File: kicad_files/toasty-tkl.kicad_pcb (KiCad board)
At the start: 2 copper layers, 345.7 x 134.1 mm, 195 parts, among them CON1 USB-MINI-B, SW0:0 ESC, SW0:10 F9, SW0:11 F10, SW0:12 F11, SW0:13 F12, SW0:14 PRINT, SW0:15 SCROLL LOCK, SW0:2 F1, SW0:3 F2, SW0:4 F3, SW0:5 F4, SW0:6 F5, SW0:7 F6, SW0:8 F7, SW0:9 F8, SW1:0 `, SW1:1 1, SW1:10 0, SW1:11 -, SW1:12 =, SW1:13 BACK SPACE, SW1:14 INSERT, SW1:15 HOME, SW1:2 2, SW1:3 3, SW1:4 4, SW1:5 5, SW1:6 6, SW1:7 7, SW1:8 8, SW1:9 9, SW2:0 TAB, SW2:1 Q, SW2:10 P, SW2:11 [, SW2:12 ], SW2:13 \, SW2:14 DELETE, SW2:15 END, SW2:2 W, SW2:3 E, SW2:4 R, SW2:5 T, SW2:6 Y, SW2:7 U, SW2:8 I, SW2:9 O, SW3:0 CAPS LOCK, SW3:1 A, SW3:10 ;, SW3:11 ', SW3:13 ENTER, SW3:14 PAGE UP, SW3:15 PAUSE, SW3:2 S, SW3:3 D, SW3:4 F, SW3:5 G, SW3:6 H, SW3:7 J, SW3:8 K, SW3:9 L, SW4:0 LEFT SHIFT, SW4:1 Z, SW4:10 /, SW4:13 RIGHT SHIFT, SW4:14 PAGE DOWN, SW4:15 UP, SW4:2 X, SW4:3 C, SW4:4 V, SW4:5 B, SW4:6 N, SW4:7 M, SW4:8 ,, SW4:9 ., SW5:0 LEFT CTRL, SW5:1 LEFT WINDOWS, SW5:10 RIGHT WINDOWS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

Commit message: Added GPL and killed some bogus cache files.
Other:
- board text added: "'"
- board text added: ","
- board text added: "-"
- board text added: "."
- board text added: "/"
- board text added: "0"
- board text added: "1"
- board text added: "2"
- board text added: "3"
- board text added: "4"
- board text added: "5"
- board text added: "6"
- board text added: "7"
- board text added: "8"
- board text added: "9"
- board text added: ";"
- board text added: "="
- board text added: "A"
- board text added: "B"
- board text added: "BACK SPACE"
- board text added: "C"
- board text added: "CAPS LOCK"
- board text added: "D"
- board text added: "DELETE"
- board text added: "DOWN"
- board text added: "E"
- board text added: "END"
- board text added: "ENTER"
- board text added: "ESC"
- board text added: "F"
- board text added: "F1"
- board text added: "F10"
- board text added: "F11"
- board text added: "F12"
- board text added: "F2"
- board text added: "F3"
- board text added: "F4"
- board text added: "F5"
- board text added: "F6"
- board text added: "F7"
- board text added: "F9"
- board text added: "G"
- board text added: "H"
- board text added: "HOME"
- board text added: "I"
- board text added: "INSERT"
- board text added: "J"
- board text added: "K"
- board text added: "L"
- board text added: "L ALT"
- board text added: "L CTRL"
- board text added: "L SHIFT"
- board text added: "L WIN"
- board text added: "LEFT"
- board text added: "M"
- board text added: "MENU"
- board text added: "N"
- board text added: "O"
- board text added: "P"
- board text added: "PAUSE"
- board text added: "PG DN"
- board text added: "PG UP"
- board text added: "PRT SC"
- board text added: "Q"
- board text added: "R"
- board text added: "R ALT"
- board text added: "R CTRL"
- board text added: "R SHIFT"
- board text added: "R WIN"
- board text added: "RIGHT"
- board text added: "S"
- board text added: "SCROLL LOCK"
- board text added: "SPACE"
- board text added: "T"
- board text added: "TAB"
- board text added: "ToastyTKL"
- board text added: "U"
- board text added: "UP"
- board text added: "V"
- board text added: "W"
- board text added: "X"
- board text added: "Y"
- board text added: "Z"
- board text added: "["
- board text added: "\"
- board text added: "]"
- board text added: "`"
- board text added: "rev 1"

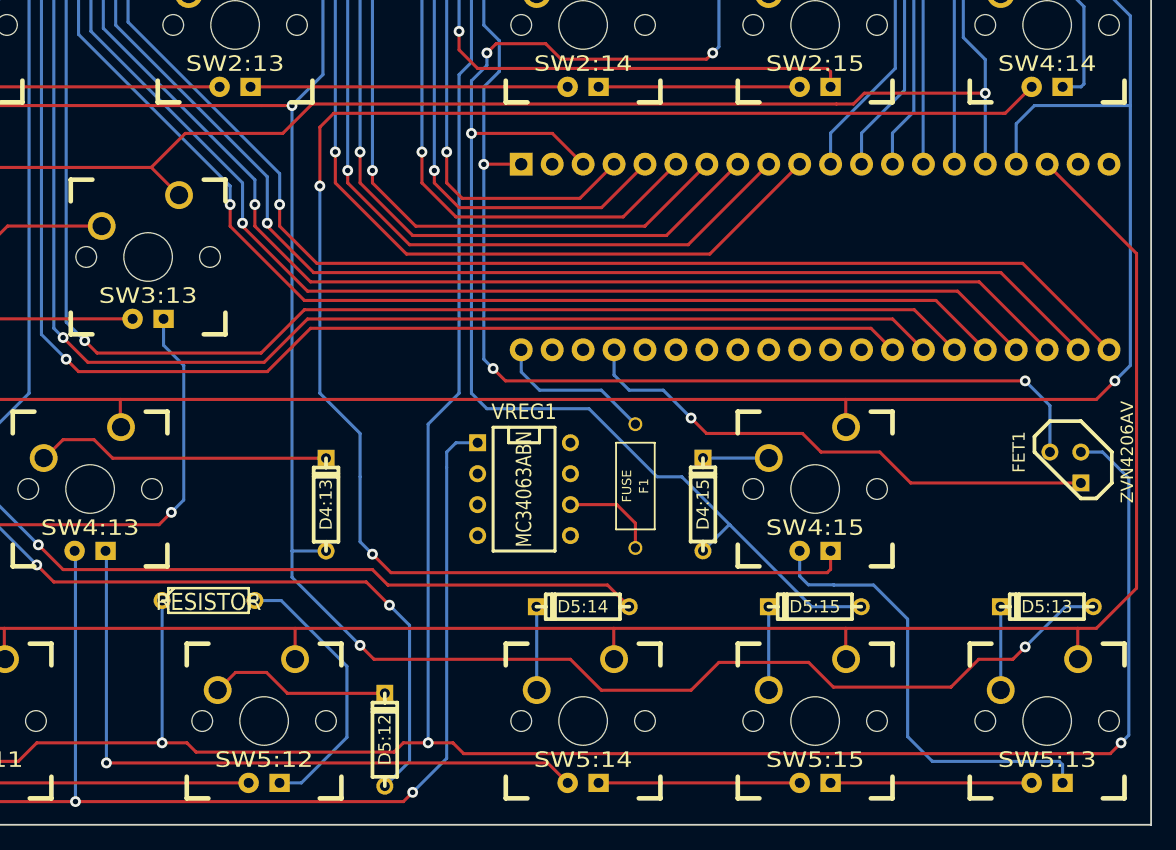
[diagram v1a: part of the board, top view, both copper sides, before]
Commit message: Updates to kicad files.  Added DXF plot altered for water jet shop.
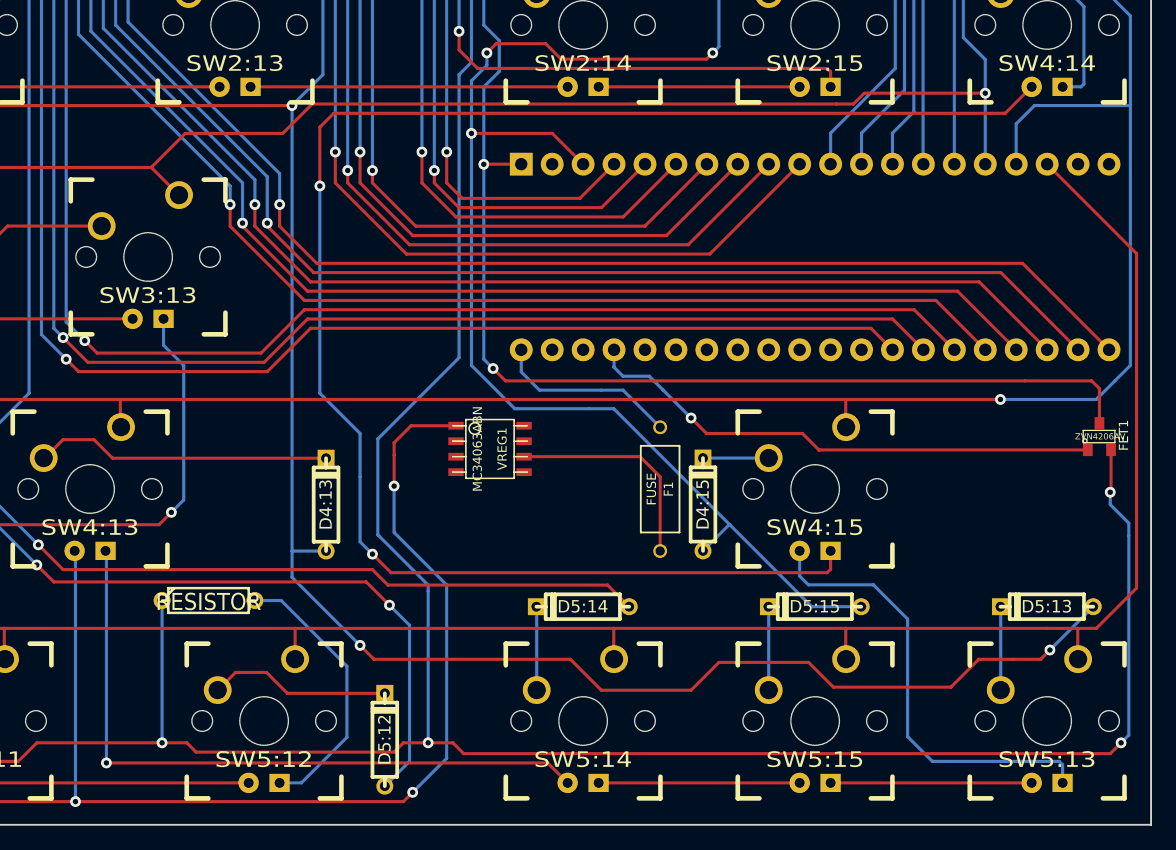
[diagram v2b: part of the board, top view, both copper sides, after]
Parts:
- FET1: footprint TO92 -> SOT23
- VREG1: footprint DIP-8__300 -> so-8
- moved VREG1 4.33 mm to (309.9, 108.7)
- moved FET1 3.78 mm to (359.9, 107.7), turned to 0 degrees
- moved F1 2.05 mm to (323.9, 112.0)
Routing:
- net N-0000090: track 8.00 -> 18.0 mm
- net /LEDCOL0: track 656.8 -> 662.2 mm, vias 5 -> 6
- net /GND: track 153.1 -> 155.6 mm, vias 4 -> 3
- net N-0000091: track 13.0 -> 15.1 mm
- net N-0000065: track 391.9 -> 393.5 mm, vias 5 -> 6
- net /COL 15: track 193.4 -> 192.0 mm
- net N-0000089: track 44.1 -> 43.2 mm

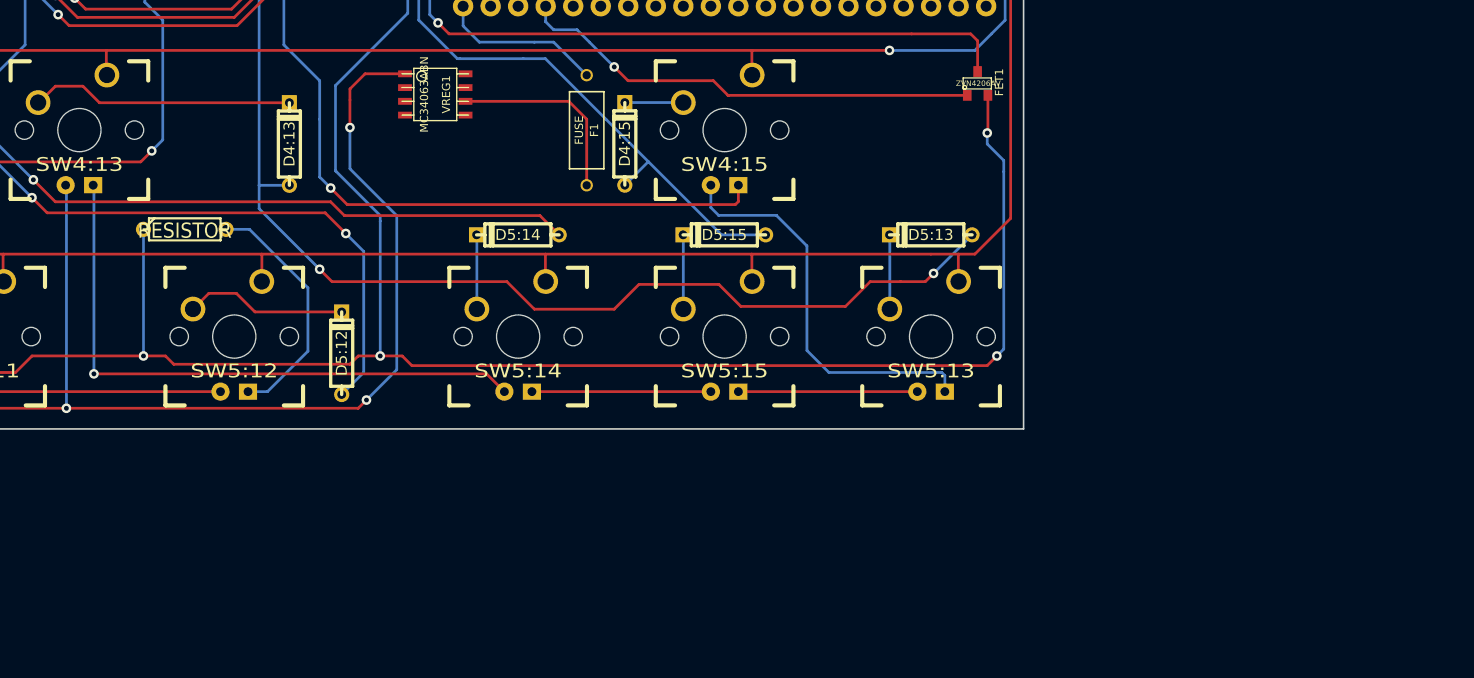
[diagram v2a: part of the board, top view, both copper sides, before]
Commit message: Fixed up my footprints, added into kicad diag.
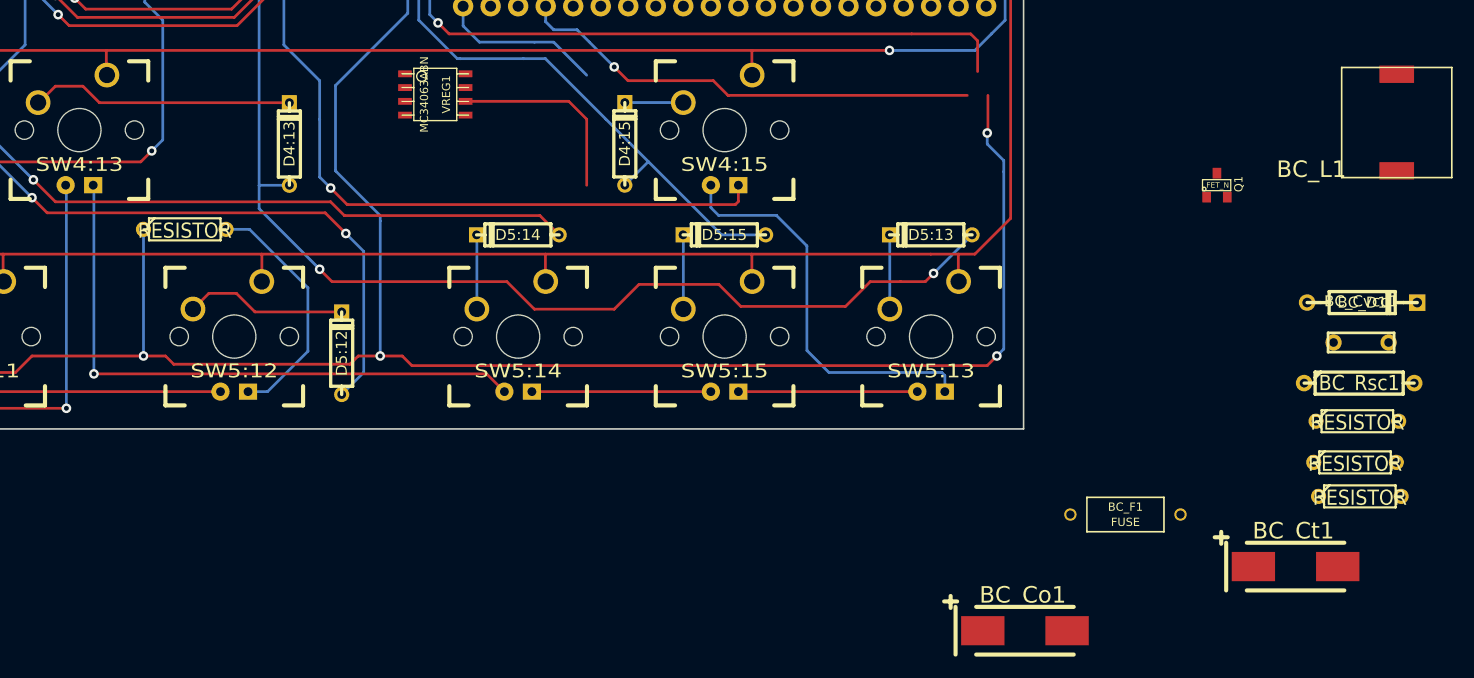
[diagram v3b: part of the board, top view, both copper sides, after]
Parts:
- removed F1: FUSE, MQ750
- removed FET1: ZVN4206AV, SOT23
- added BC_Co1: CP1, TantalC_SizeD_EIA-7343_HandSoldering_RevA_28Aug2012, F.Cu at (364.3, 158.2)
- added BC_Ct1: CP1, TantalC_SizeD_EIA-7343_HandSoldering_RevA_28Aug2012, F.Cu at (389.3, 152.3)
- added BC_Cvcc1: CP1, CP_6mm, F.Cu at (395.3, 131.6)
- added BC_D1: DIODE, DO-41, F.Cu at (395.4, 127.9)
- added BC_F1: FUSE, MQ750, F.Cu at (373.6, 147.5)
- added BC_L1: INDUCTOR, SCRH103R, F.Cu at (398.6, 111.3)
- added BC_R0: RESISTOR, R3, F.Cu at (395.2, 145.8)
- added BC_R1: RESISTOR, R3, F.Cu at (395.0, 138.9)
- added BC_R2: RESISTOR, R3, F.Cu at (394.7, 142.7)
- added BC_Rsc1: RESISTOR, R4, F.Cu at (395.1, 135.3)
- added Q1: FET_N, SOT23, F.Cu at (382.0, 117.1)
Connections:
- R10 pad 1: N-0000065 (its old number) -> N-0000071
- R11 pad 1: N-0000065 (its old number) -> N-0000071
- R12 pad 1: N-0000065 (its old number) -> (no net)
- R2 pad 1: N-0000065 (its old number) -> N-0000071
- R3 pad 1: N-0000065 (its old number) -> N-0000071
- R4 pad 1: N-0000065 (its old number) -> N-0000071
- R5 pad 1: N-0000065 (its old number) -> N-0000071
- R6 pad 1: N-0000065 (its old number) -> N-0000071
- R7 pad 1: N-0000065 (its old number) -> N-0000071
- R8 pad 1: N-0000065 (its old number) -> N-0000071
- R9 pad 1: N-0000065 (its old number) -> N-0000071
- VREG1 pad 1: /LEDCOL0 -> N-0000098
- VREG1 pad 2: (no net) -> /GND
- VREG1 pad 3: (no net) -> N-0000091
- VREG1 pad 4: (no net) -> /GND
- VREG1 pad 5: (no net) -> N-0000090
- VREG1 pad 7: (no net) -> N-0000099
- VREG1 pad 8: (no net) -> N-00000100
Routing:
- net N-0000071: track 0.00 -> 393.5 mm, vias 0 -> 6
- net N-0000065 (its old number): track 393.5 -> 0.00 mm, vias 6 -> 0
- net /LEDCOL0: track 662.2 -> 596.9 mm, vias 6 -> 4

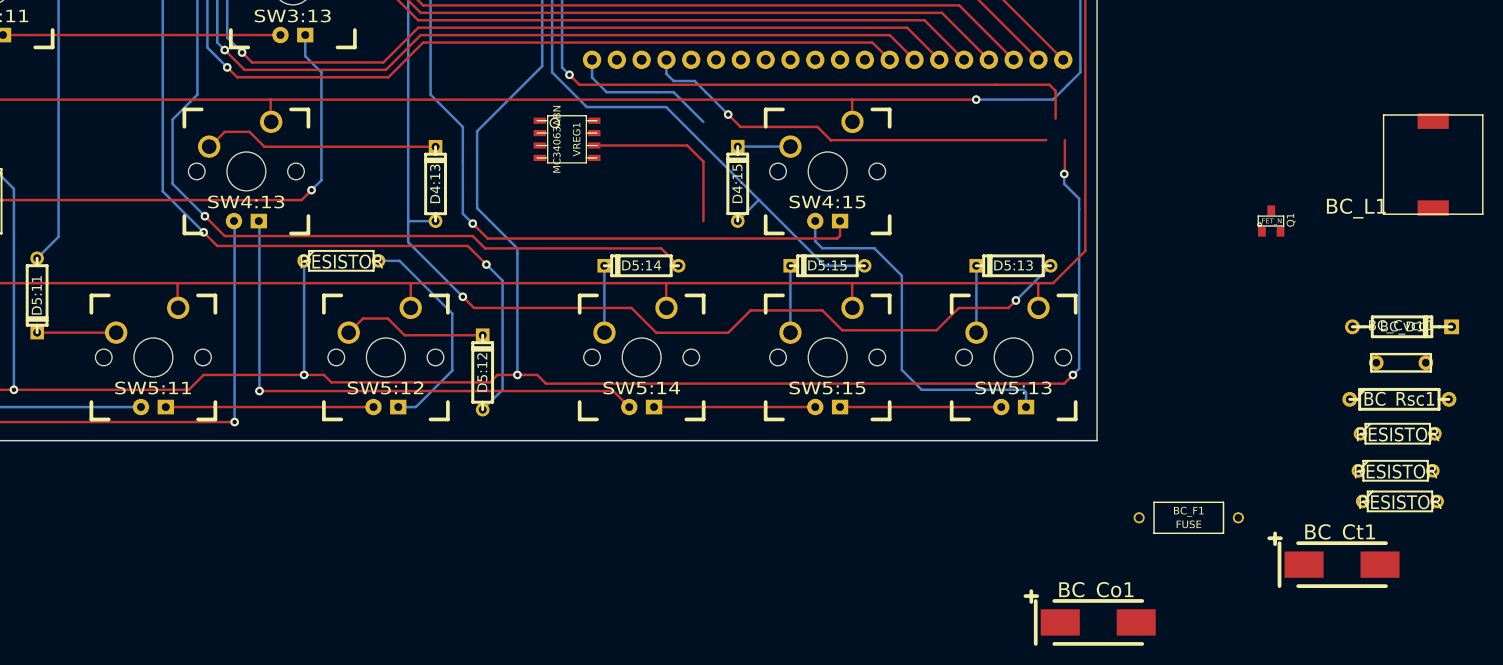
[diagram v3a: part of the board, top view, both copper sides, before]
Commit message: Did some preliminary traces for boost converter circuit.
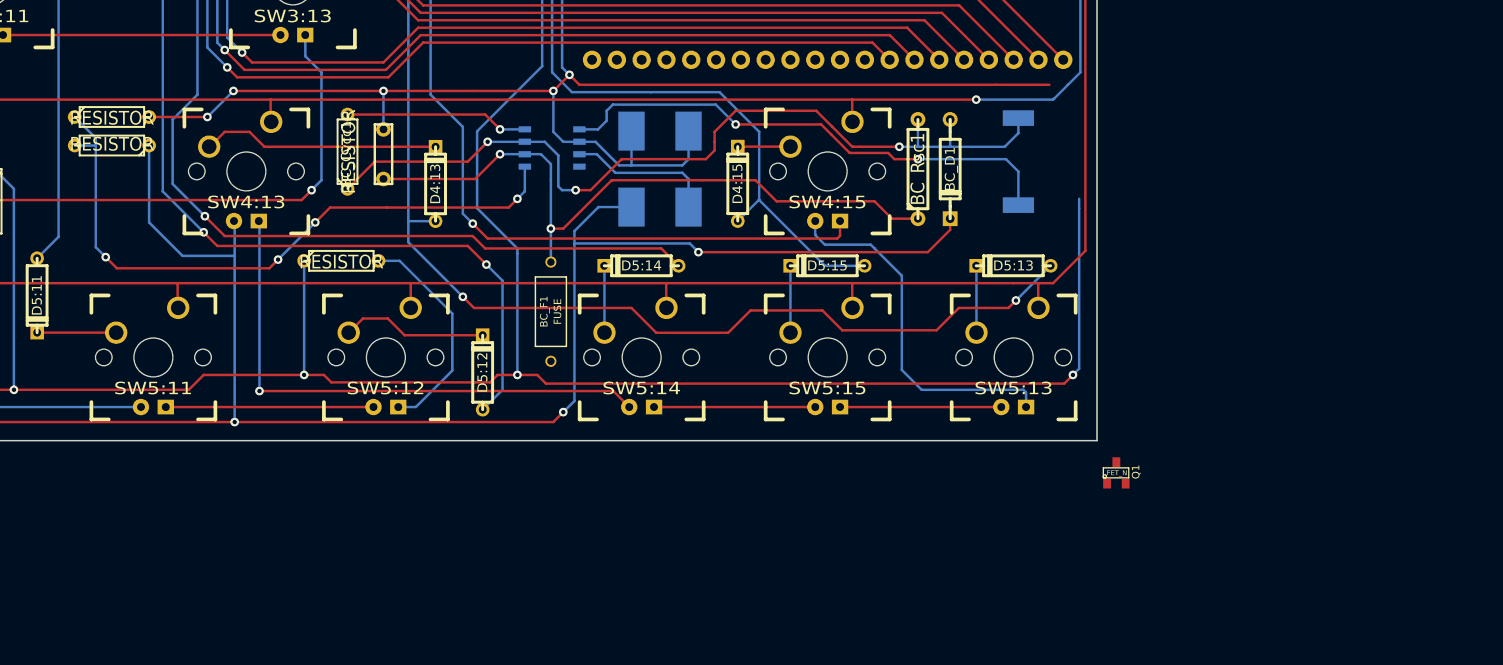
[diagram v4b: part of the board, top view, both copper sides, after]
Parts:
- BC_Co1, BC_Ct1, BC_L1, VREG1: moved to B.Cu
- moved BC_R2 135.6 mm to (263.3, 109.3), turned to 180 degrees
- moved BC_R1 135.6 mm to (263.3, 106.4)
- moved BC_R0 113.6 mm to (287.4, 110.0), turned to 90 degrees
- moved BC_Cvcc1 106.4 mm to (291.1, 110.2), turned to 90 degrees
- moved BC_Ct1 78.2 mm to (322.3, 111.8), turned to 90 degrees
- moved BC_F1 68.7 mm to (308.2, 126.4), turned to 270 degrees
- moved BC_Co1 66.6 mm to (316.5, 111.8), turned to 90 degrees
- moved BC_Rsc1 54.7 mm to (345.8, 111.8), turned to 90 degrees
- moved BC_D1 49.0 mm to (349.1, 111.8), turned to 270 degrees
- moved BC_L1 42.5 mm to (356.1, 111.0)
- moved Q1 30.3 mm to (366.1, 142.9)
- moved VREG1 1.76 mm to (308.4, 109.6)
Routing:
- net /LEDCOL0: track 596.9 -> 715.9 mm, vias 4 -> 6
- net N-0000099: track 0.00 -> 88.3 mm, vias 0 -> 3
- net /GND: track 155.6 -> 226.7 mm, vias 3 -> 7
- net N-0000090: track 0.00 -> 67.0 mm, vias 0 -> 4
- net N-0000098: track 0.00 -> 52.9 mm, vias 0 -> 2
- net N-0000092: track 18.0 -> 69.9 mm, vias 0 -> 2
- net N-0000097: track 43.2 -> 0.00 mm, vias 1 -> 0
- net N-00000100: track 0.00 -> 18.8 mm, vias 0 -> 1
- net N-0000094: track 15.1 -> 0.00 mm
- net N-0000091: track 0.00 -> 15.1 mm
- net N-0000071: track 393.5 -> 386.8 mm, vias 6 -> 5
- net /COL 15: track 192.0 -> 196.1 mm

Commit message: Fixed fet pins.
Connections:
- Q1 pad 1: (no net) -> N-0000097
- Q1 pad 2: (no net) -> /GND
- Q1 pad 3: (no net) -> N-0000071
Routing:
- net N-0000071: track 386.8 -> 310.6 mm, vias 5 -> 4
- net /GND: track 226.7 -> 182.2 mm, vias 7 -> 6
- net N-0000099: track 88.3 -> 81.2 mm
- net N-0000092: track 69.9 -> 67.9 mm
- net N-0000098: track 52.9 -> 51.0 mm
- net /COL 15: track 196.1 -> 197.9 mm
